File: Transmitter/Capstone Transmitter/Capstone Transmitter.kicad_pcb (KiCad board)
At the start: 2 copper layers, 150 x 60 mm, 38 parts, among them J1 Conn_01x04, J2 Conn_01x04, J3 RIGHT, LEFT, J4 UP,DOWN, J5 BTN1, BTN2, J6 AnalogStick Pot1 +/-, J7 AnalogStick Pot2 +/-, Q1 DMP3099L, U2 TPS63020DSJR, U3 ESP32-WROOM-32UE

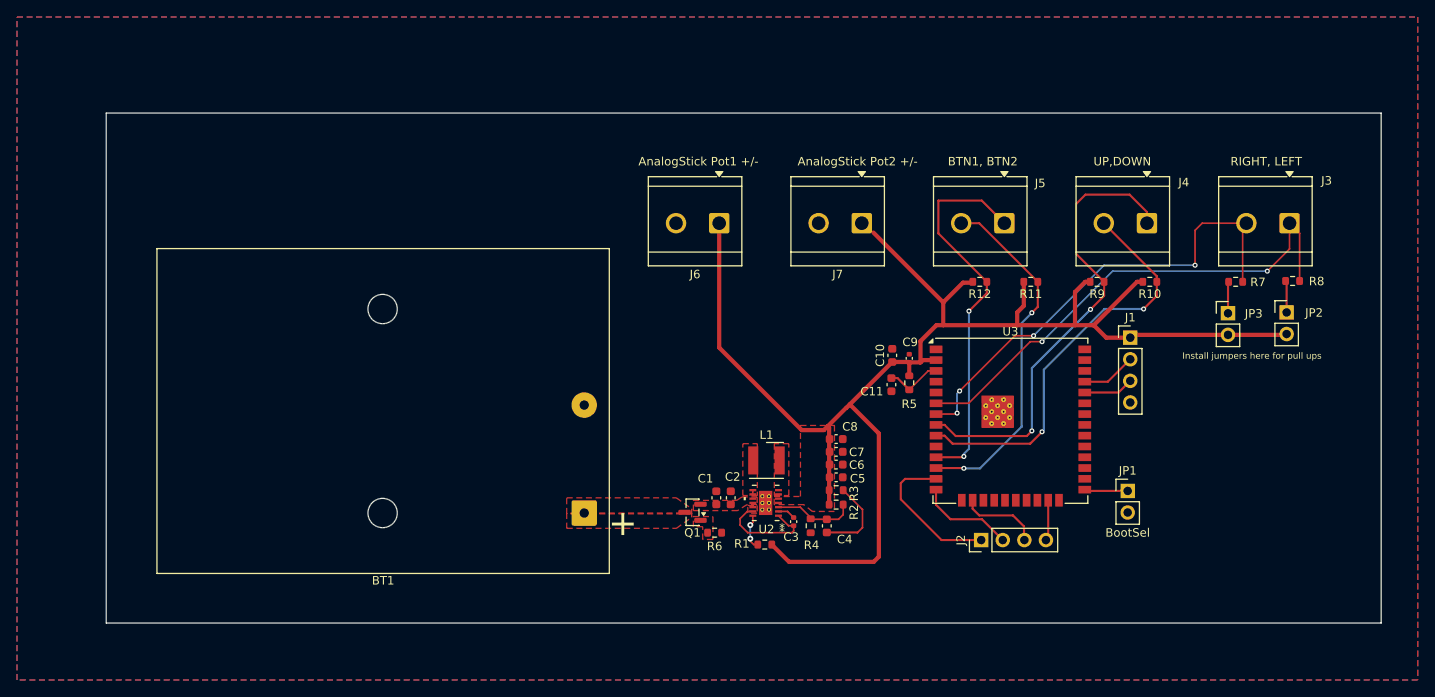
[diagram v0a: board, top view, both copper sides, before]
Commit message: Moved battery around and added screw terminals for End of Travel (EoT) indicators
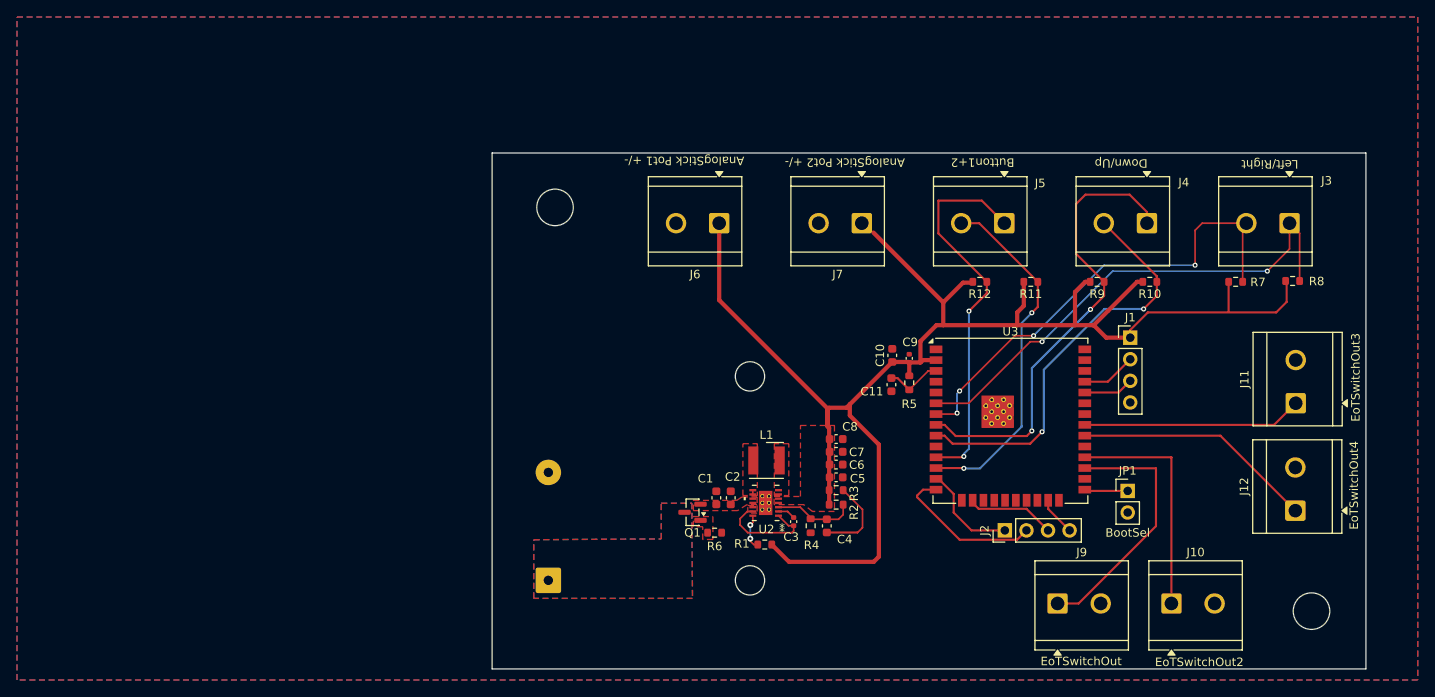
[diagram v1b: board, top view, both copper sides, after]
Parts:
- removed JP2: Pull up Jumper 1, Connector_PinHeader_2.54mm:PinHeader_1x02_P2.54mm_Vertical
- removed JP3: Pull up Jumper 2, Connector_PinHeader_2.54mm:PinHeader_1x02_P2.54mm_Vertical
- added J10: EoTSwitchOut2, TerminalBlock_CUI:TerminalBlock_CUI_TB007-508-02_1x02_P5.08mm_Horizontal, F.Cu at (187.0, 98.6)
- added J11: EoTSwitchOut3, TerminalBlock_CUI:TerminalBlock_CUI_TB007-508-02_1x02_P5.08mm_Horizontal, F.Cu at (201.6, 75.0)
- added J12: EoTSwitchOut4, TerminalBlock_CUI:TerminalBlock_CUI_TB007-508-02_1x02_P5.08mm_Horizontal, F.Cu at (201.6, 87.7)
- added J9: EoTSwitchOut, TerminalBlock_CUI:TerminalBlock_CUI_TB007-508-02_1x02_P5.08mm_Horizontal, F.Cu at (173.6, 98.6)
- added REF**: MountingHole_4.3mm_M4, MountingHole:MountingHole_4.3mm_M4, F.Cu at (203.5, 99.5)
- added REF**: MountingHole_4.3mm_M4, MountingHole:MountingHole_4.3mm_M4, F.Cu at (114.5, 52.0)
- BT1: moved to B.Cu
- J3: value RIGHT, LEFT -> Left/Right
- J4: value UP,DOWN -> Down/Up
- J5: value BTN1, BTN2 -> Button1+2
- Q1: value DMP3099L -> DMP2035U
- moved BT1 8.98 mm to (113.7, 95.9), turned to 0 degrees
- moved J2 3.01 mm to (167.4, 90.0)
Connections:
- R7 pad 2: Net-(JP3-A) -> +3.3V
- R8 pad 2: Net-(JP2-A) -> +3.3V
- U3 pad 27: unconnected-(U3-IO16-Pad27) -> /EoTLED1
- U3 pad 28: unconnected-(U3-IO17-Pad28) -> /EoTLED2
- U3 pad 30: unconnected-(U3-IO18-Pad30) -> /EoTLED4
- U3 pad 31: unconnected-(U3-IO19-Pad31) -> /EoTLED3
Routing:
- net /EoTLED1: track 0.00 -> 30.5 mm
- net /EoTLED4: track 0.00 -> 28.4 mm
- net /EoTLED2: track 0.00 -> 26.1 mm
- net /EoTLED3: track 0.00 -> 25.9 mm
- net +3.3V: track 175.7 -> 183.3 mm
- net /JTAG_TDI: track 11.3 -> 18.1 mm
- net /JTAG_TMS: track 17.7 -> 11.9 mm
- net Net-(JP2-A): track 3.75 -> 0.00 mm
- net Net-(JP3-A): track 3.73 -> 0.00 mm
- net /JTAG_TCK: track 9.52 -> 10.5 mm
- added copper zone on B.Cu, net Net-(BT1-+)
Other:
- board size 150 x 60 mm -> 102.8 x 60.7 mm
- copper layers 2 -> 4
- board text removed: "Install jumpers here for pull ups"
